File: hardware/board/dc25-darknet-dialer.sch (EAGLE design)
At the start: 62 parts

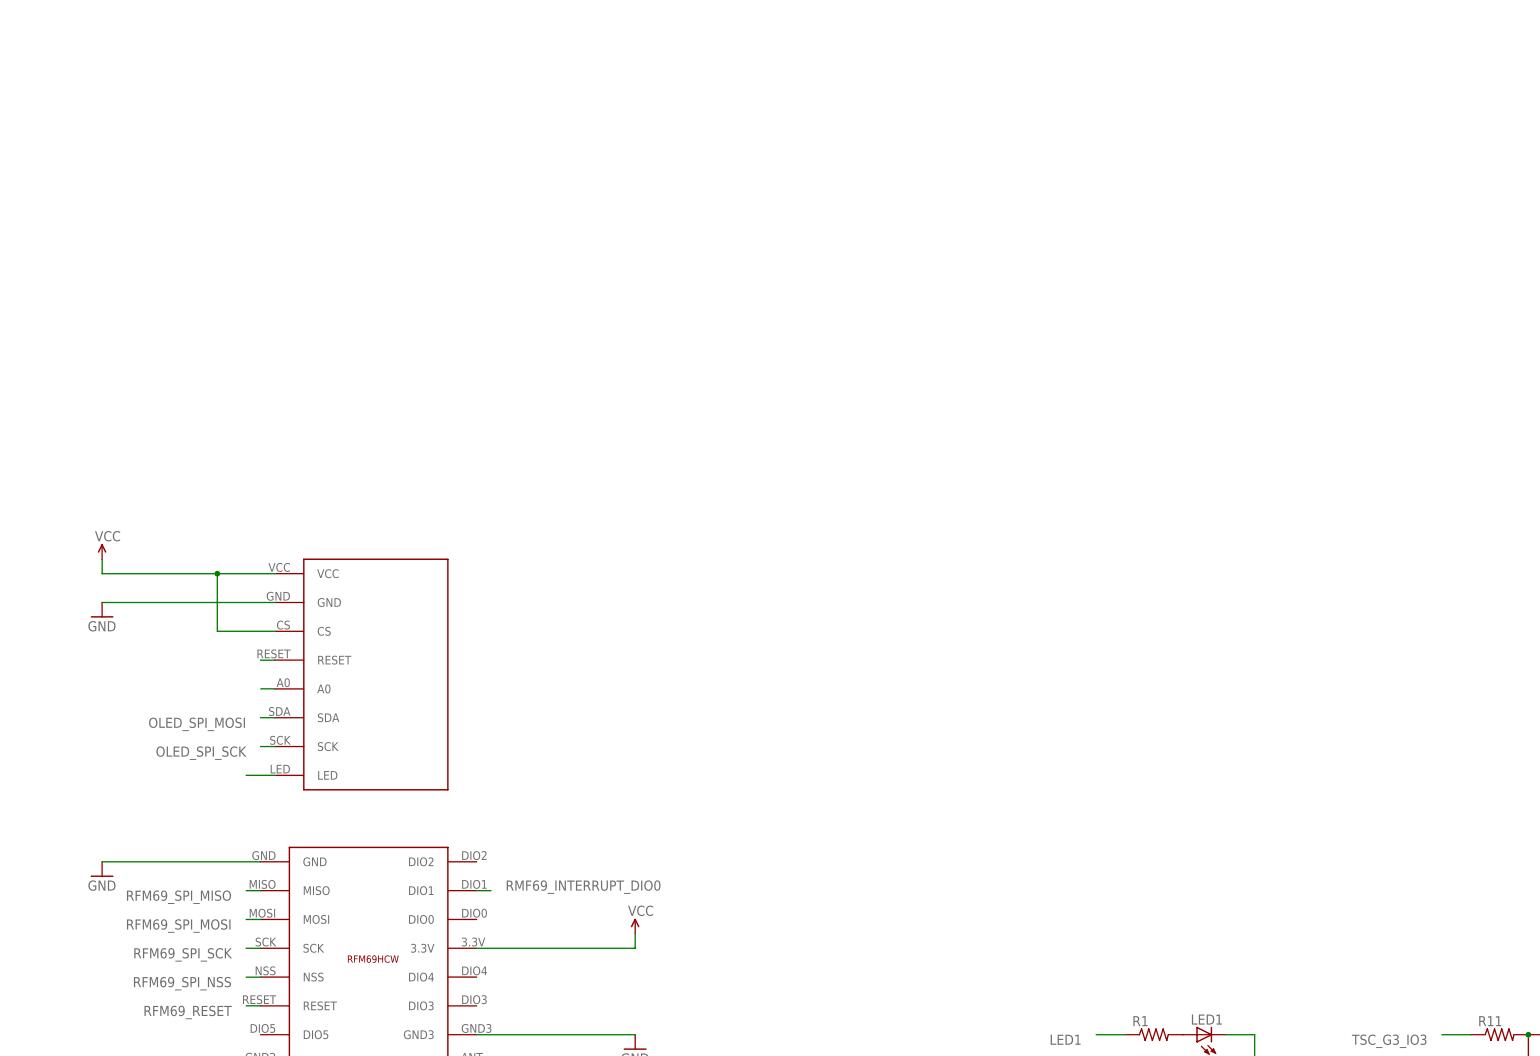
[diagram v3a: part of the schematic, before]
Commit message: Added power and IR
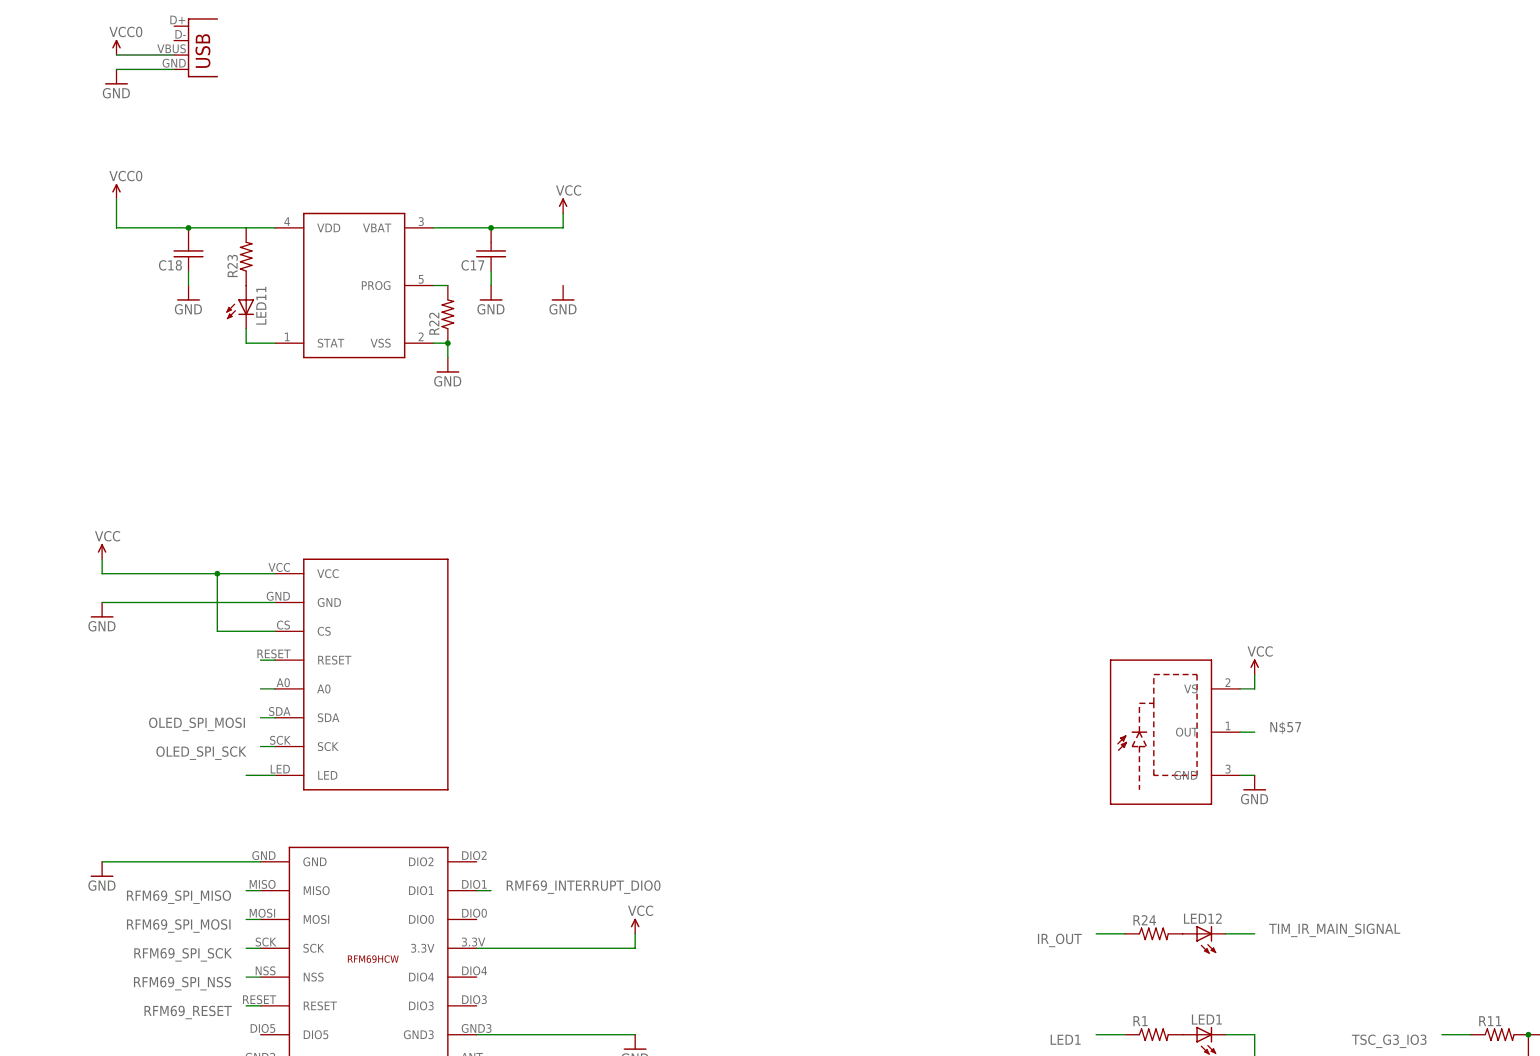
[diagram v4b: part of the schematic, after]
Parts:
- added C17, C18: (no value), SYNShop:C-USC0603
- added LED11: (no value), SYNShop:LED0603
- added LED12: (no value), SYNShop:LED5MM
- added R22, R23: (no value), SYNShop:R-US_R0603
- added R24: (no value), SYNShop:R-US_0309/12
- added U$11: DS21984E, darknet_parts_library:DS21984E
- added U$17: SOP22, SYNShop:SOP22
- added X1: USB-MICROB, SYNShop:USB-MICROB
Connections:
- new net N$22: R22.2, U$11.PROG
- new net N$23: LED12.A, R24.2
- new net N$24: LED11.A, R23.1
- new net N$25: LED11.C, U$11.STAT
- new net VCC0: C18.2, R23.2, U$11.VDD, X1.VBUS
- net GND: now also C17.1, C18.1, R22.1, U$11.VSS, U$17.GND, X1.GND
- net IR_OUT: now also R24.1
- net N$57: now also U$17.OUT
- net TIM_IR_MAIN_SIGNAL: now also LED12.C
- net VCC: now also C17.2, U$11.VBAT, U$17.VS
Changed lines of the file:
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@@
 <part name="U$10" library="SYNShop" deviceset="VCC" device=""/>
 <part name="C16" library="SYNShop" deviceset="C-US" device="C0603" value="4.7uF"/>
+<part name="U$11" library="darknet_parts_library" deviceset="DS21984E" device=""/>
+<part name="R22" library="SYNShop" deviceset="R-US_" device="R0603"/>
+<part name="GND22" library="SYNShop" deviceset="GND" device=""/>
+<part name="GND23" library="SYNShop" deviceset="GND" device=""/>
+<part name="R23" library="SYNShop" deviceset="R-US_" device="R0603"/>
+<part name="LED11" library="SYNShop" deviceset="LED" device="0603"/>
+<part name="C17" library="SYNShop" deviceset="C-US" device="C0603"/>
+<part name="GND24" library="SYNShop" deviceset="GND" device=""/>
+<part name="U$13" library="SYNShop" deviceset="VCC" device=""/>
+<part name="U$14" library="SYNShop" deviceset="VCC0" device=""/>
+<part name="C18" library="SYNShop" deviceset="C-US" device="C0603"/>
+<part name="GND25" library="SYNShop" deviceset="GND" device=""/>
+<part name="X1" library="SYNShop" deviceset="USB" device="-MICROB"/>
+<part name="U$16" library="SYNShop" deviceset="VCC0" device=""/>
+<part name="GND26" library="SYNShop" deviceset="GND" device=""/>
+<part name="U$17" library="SYNShop" deviceset="SOP22" device=""/>
+<part name="LED12" library="SYNShop" deviceset="LED" device="5MM"/>
+<part name="R24" library="SYNShop" deviceset="R-US_" device="0309/12"/>
+<part name="GND27" library="SYNShop" deviceset="GND" device=""/>
+<part name="U$18" library="SYNShop" deviceset="VCC" device=""/>
 </parts>
 <sheets>
@@
 <instance part="U$10" gate="G$1" x="114.3" y="144.78"/>
 <instance part="C16" gate="G$1" x="73.66" y="139.7" rot="R180"/>
+<instance part="U$11" gate="G$1" x="43.18" y="322.58"/>
+<instance part="R22" gate="G$1" x="58.42" y="317.5" rot="R90"/>
+<instance part="GND22" gate="1" x="58.42" y="307.34"/>
+<instance part="GND23" gate="1" x="66.04" y="320.04"/>
+<instance part="R23" gate="G$1" x="22.86" y="327.66" rot="R90"/>
+<instance part="LED11" gate="G$1" x="22.86" y="320.04"/>
+<instance part="C17" gate="G$1" x="66.04" y="327.66" rot="R180"/>
+<instance part="GND24" gate="1" x="78.74" y="320.04"/>
+<instance part="U$13" gate="G$1" x="78.74" y="335.28"/>
+<instance part="U$14" gate="VCC0" x="0" y="337.82"/>
+<instance part="C18" gate="G$1" x="12.7" y="327.66" rot="R180"/>
+<instance part="GND25" gate="1" x="12.7" y="320.04"/>
+<instance part="X1" gate="G$1" x="12.7" y="360.68"/>
+<instance part="U$16" gate="VCC0" x="0" y="363.22"/>
+<instance part="GND26" gate="1" x="0" y="358.14"/>
+<instance part="U$17" gate="G$1" x="185.42" y="243.84"/>
+<instance part="LED12" gate="G$1" x="190.5" y="208.28" rot="R90"/>
+<instance part="R24" gate="G$1" x="182.88" y="208.28"/>
+<instance part="GND27" gate="1" x="200.66" y="233.68"/>
+<instance part="U$18" gate="G$1" x="200.66" y="254"/>
 </instances>
 <busses>
@@
 <junction x="83.82" y="137.16"/>
 </segment>
+<segment>
+<pinref part="U$11" gate="G$1" pin="VSS"/>
+<pinref part="R22" gate="G$1" pin="1"/>
+<wire x1="55.88" y1="312.42" x2="58.42" y2="312.42" width="0.1524" layer="91"/>
+<pinref part="GND22" gate="1" pin="GND"/>
+<wire x1="58.42" y1="312.42" x2="58.42" y2="309.88" width="0.1524" layer="91"/>
+<junction x="58.42" y="312.42"/>
+</segment>
+<segment>
+<pinref part="C17" gate="G$1" pin="1"/>
+<pinref part="GND23" gate="1" pin="GND"/>
+<wire x1="66.04" y1="322.58" x2="66.04" y2="325.12" width="0.1524" layer="91"/>
+</segment>
+<segment>
+<pinref part="C18" gate="G$1" pin="1"/>
+<pinref part="GND25" gate="1" pin="GND"/>
+<wire x1="12.7" y1="322.58" x2="12.7" y2="325.12" width="0.1524" layer="91"/>
+</segment>
+<segment>
+<pinref part="X1" gate="G$1" pin="GND"/>
+<pinref part="GND26" gate="1" pin="GND"/>
+<wire x1="10.16" y1="360.68" x2="0" y2="360.68" width="0.1524" layer="91"/>
+</segment>
+<segment>
+<pinref part="U$17" gate="G$1" pin="GND"/>
+<pinref part="GND27" gate="1" pin="GND"/>
+<wire x1="198.12" y1="236.22" x2="200.66" y2="236.22" width="0.1524" layer="91"/>
+</segment>
 </net>
 <net name="N$12" class="0">
@@
 <junction x="83.82" y="144.78"/>
 </segment>
+<segment>
+<pinref part="U$11" gate="G$1" pin="VBAT"/>
+<wire x1="55.88" y1="332.74" x2="66.04" y2="332.74" width="0.1524" layer="91"/>
+<pinref part="C17" gate="G$1" pin="2"/>
+<wire x1="66.04" y1="332.74" x2="78.74" y2="332.74" width="0.1524" layer="91"/>
+<junction x="66.04" y="332.74"/>
+<pinref part="U$13" gate="G$1" pin="VCC"/>
+<wire x1="78.74" y1="332.74" x2="78.74" y2="335.28" width="0.1524" layer="91"/>
+</segment>
+<segment>
+<pinref part="U$17" gate="G$1" pin="VS"/>
+<pinref part="U$18" gate="G$1" pin="VCC"/>
+<wire x1="198.12" y1="251.46" x2="200.66" y2="251.46" width="0.1524" layer="91"/>
+<wire x1="200.66" y1="251.46" x2="200.66" y2="254" width="0.1524" layer="91"/>
+</segment>
 </net>
 <net name="TSC_G3_IO2" class="0">
@@
 <label x="15.24" y="137.16" size="1.778" layer="95" rot="R90"/>
 </segment>
+<segment>
+<pinref part="R24" gate="G$1" pin="1"/>
+<wire x1="177.8" y1="208.28" x2="172.72" y2="208.28" width="0.1524" layer="91"/>
+<label x="170.18" y="208.28" size="1.778" layer="95" rot="R180"/>
+</segment>
 </net>
 <net name="RCC_OSC_IN" class="0">
@@
 <label x="17.78" y="137.16" size="1.778" layer="95" rot="R90"/>
 </segment>
+<segment>
+<pinref part="LED12" gate="G$1" pin="C"/>
+<wire x1="195.58" y1="208.28" x2="200.66" y2="208.28" width="0.1524" layer="91"/>
+<label x="203.2" y="208.28" size="1.778" layer="95"/>
+</segment>
 </net>
 <net name="TSC_G5_IO4" class="0">
@@
 <label x="-10.16" y="99.06" size="1.778" layer="95" rot="R180"/>
 </segment>
+<segment>
+<pinref part="U$17" gate="G$1" pin="OUT"/>
+<wire x1="198.12" y1="243.84" x2="200.66" y2="243.84" width="0.1524" layer="91"/>
+<label x="203.2" y="243.84" size="1.778" layer="95"/>
+</segment>
 </net>
 <net name="N$58" class="0">
@@
 </segment>
 </net>
+<net name="N$22" class="0">
+<segment>
+<pinref part="U$11" gate="G$1" pin="PROG"/>
+<pinref part="R22" gate="G$1" pin="2"/>
+<wire x1="55.88" y1="322.58" x2="58.42" y2="322.58" width="0.1524" layer="91"/>
+</segment>
+</net>
+<net name="N$24" class="0">
+<segment>
+<pinref part="R23" gate="G$1" pin="1"/>
+<pinref part="LED11" gate="G$1" pin="A"/>
+</segment>
+</net>
+<net name="N$25" class="0">
+<segment>
+<pinref part="LED11" gate="G$1" pin="C"/>
+<wire x1="22.86" y1="314.96" x2="22.86" y2="312.42" width="0.1524" layer="91"/>
+<pinref part="U$11" gate="G$1" pin="STAT"/>
+<wire x1="22.86" y1="312.42" x2="27.94" y2="312.42" width="0.1524" layer="91"/>
+</segment>
+</net>
+<net name="VCC0" class="0">
+<segment>
+<pinref part="U$11" gate="G$1" pin="VDD"/>
+<pinref part="R23" gate="G$1" pin="2"/>
+<wire x1="27.94" y1="332.74" x2="22.86" y2="332.74" width="0.1524" layer="91"/>
+<wire x1="22.86" y1="332.74" x2="12.7" y2="332.74" width="0.1524" layer="91"/>
+<pinref part="C18" gate="G$1" pin="2"/>
+<junction x="12.7" y="332.74"/>
+<wire x1="12.7" y1="332.74" x2="0" y2="332.74" width="0.1524" layer="91"/>
+<pinref part="U$14" gate="VCC0" pin="VCC0"/>
+<wire x1="0" y1="332.74" x2="0" y2="337.82" width="0.1524" layer="91"/>
+</segment>
+<segment>
+<pinref part="U$16" gate="VCC0" pin="VCC0"/>
+<pinref part="X1" gate="G$1" pin="VBUS"/>
+<wire x1="0" y1="363.22" x2="10.16" y2="363.22" width="0.1524" layer="91"/>
+</segment>
+</net>
+<net name="N$23" class="0">
+<segment>
+<pinref part="R24" gate="G$1" pin="2"/>
+<pinref part="LED12" gate="G$1" pin="A"/>
+</segment>
+</net>

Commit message: Updated power, wired IR
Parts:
- added C19, C20: (no value), SYNShop:C-USC0603
- added CN1: (no value), adafruit:JST_2PIN-THM-RA
- added L1: (no value), dp_devices:FERRITE-0603
- added R25: (no value), SYNShop:R-US_0309/12
- added R26, R27: (no value), SYNShop:R-US_R0603
- added SW1: RESET, SYNShop:SWITCH_TACTILETACTILE-2PIN-NARROW
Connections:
- new net N$26: C19.2, R27.1, X1.D+
- new net N$27: C20.2, R26.1, X1.D-
- new net N$28: L1.2, X1.VBUS
- net GND: now also C19.1, C20.1, CN1.2, SW1.C
- net RESET: now also R25.1, SW1.A
- net VCC: now also CN1.1, R25.2
- net VCC0: now also L1.1; no longer X1.VBUS
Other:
- note added: "Note need to check on power connection / battery"
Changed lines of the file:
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@@
 <part name="X1" library="SYNShop" deviceset="USB" device="-MICROB"/>
 <part name="U$16" library="SYNShop" deviceset="VCC0" device=""/>
-<part name="GND26" library="SYNShop" deviceset="GND" device=""/>
 <part name="U$17" library="SYNShop" deviceset="SOP22" device=""/>
 <part name="LED12" library="SYNShop" deviceset="LED" device="5MM"/>
@@
 <part name="GND27" library="SYNShop" deviceset="GND" device=""/>
 <part name="U$18" library="SYNShop" deviceset="VCC" device=""/>
+<part name="CN1" library="adafruit" deviceset="JST_2PIN" device="-THM-RA"/>
+<part name="SW1" library="SYNShop" deviceset="SWITCH_TACTILE" device="TACTILE-2PIN-NARROW" value="RESET"/>
+<part name="R25" library="SYNShop" deviceset="R-US_" device="0309/12"/>
+<part name="GND28" library="SYNShop" deviceset="GND" device=""/>
+<part name="U$20" library="SYNShop" deviceset="VCC" device=""/>
+<part name="R26" library="SYNShop" deviceset="R-US_" device="R0603"/>
+<part name="R27" library="SYNShop" deviceset="R-US_" device="R0603"/>
+<part name="C19" library="SYNShop" deviceset="C-US" device="C0603"/>
+<part name="C20" library="SYNShop" deviceset="C-US" device="C0603"/>
+<part name="L1" library="dp_devices" deviceset="FERRITE" device="-0603"/>
+<part name="GND26" library="SYNShop" deviceset="GND" device=""/>
 </parts>
 <sheets>
 <sheet>
 <plain>
+<text x="99.06" y="317.5" size="1.778" layer="91">Note need to check on power connection / battery</text>
 </plain>
 <instances>
@@
 <instance part="C18" gate="G$1" x="12.7" y="327.66" rot="R180"/>
 <instance part="GND25" gate="1" x="12.7" y="320.04"/>
-<instance part="X1" gate="G$1" x="12.7" y="360.68"/>
-<instance part="U$16" gate="VCC0" x="0" y="363.22"/>
-<instance part="GND26" gate="1" x="0" y="358.14"/>
+<instance part="X1" gate="G$1" x="55.88" y="360.68"/>
+<instance part="U$16" gate="VCC0" x="0" y="365.76"/>
 <instance part="U$17" gate="G$1" x="185.42" y="243.84"/>
 <instance part="LED12" gate="G$1" x="190.5" y="208.28" rot="R90"/>
@@
 <instance part="GND27" gate="1" x="200.66" y="233.68"/>
 <instance part="U$18" gate="G$1" x="200.66" y="254"/>
+<instance part="CN1" gate="G$1" x="104.14" y="330.2"/>
+<instance part="SW1" gate="G$1" x="27.94" y="396.24"/>
+<instance part="R25" gate="G$1" x="27.94" y="406.4" rot="R90"/>
+<instance part="GND28" gate="1" x="27.94" y="388.62"/>
+<instance part="U$20" gate="G$1" x="27.94" y="411.48"/>
+<instance part="R26" gate="G$1" x="17.78" y="375.92" rot="R180"/>
+<instance part="R27" gate="G$1" x="17.78" y="381" rot="R180"/>
+<instance part="C19" gate="G$1" x="33.02" y="368.3" rot="R180"/>
+<instance part="C20" gate="G$1" x="25.4" y="368.3" rot="R180"/>
+<instance part="L1" gate="L" x="15.24" y="363.22" rot="R90"/>
+<instance part="GND26" gate="1" x="33.02" y="355.6"/>
 </instances>
 <busses>
@@
 </segment>
 <segment>
-<pinref part="X1" gate="G$1" pin="GND"/>
-<pinref part="GND26" gate="1" pin="GND"/>
-<wire x1="10.16" y1="360.68" x2="0" y2="360.68" width="0.1524" layer="91"/>
-</segment>
-<segment>
 <pinref part="U$17" gate="G$1" pin="GND"/>
 <pinref part="GND27" gate="1" pin="GND"/>
 <wire x1="198.12" y1="236.22" x2="200.66" y2="236.22" width="0.1524" layer="91"/>
 </segment>
+<segment>
+<pinref part="CN1" gate="G$1" pin="2"/>
+<pinref part="GND24" gate="1" pin="GND"/>
+<wire x1="101.6" y1="330.2" x2="78.74" y2="330.2" width="0.1524" layer="91"/>
+<wire x1="78.74" y1="330.2" x2="78.74" y2="322.58" width="0.1524" layer="91"/>
+</segment>
+<segment>
+<pinref part="X1" gate="G$1" pin="GND"/>
+<wire x1="53.34" y1="360.68" x2="33.02" y2="360.68" width="0.1524" layer="91"/>
+<pinref part="C20" gate="G$1" pin="1"/>
+<wire x1="33.02" y1="360.68" x2="25.4" y2="360.68" width="0.1524" layer="91"/>
+<wire x1="25.4" y1="365.76" x2="25.4" y2="360.68" width="0.1524" layer="91"/>
+<pinref part="C19" gate="G$1" pin="1"/>
+<wire x1="33.02" y1="365.76" x2="33.02" y2="360.68" width="0.1524" layer="91"/>
+<junction x="33.02" y="360.68"/>
+<pinref part="GND26" gate="1" pin="GND"/>
+<wire x1="33.02" y1="358.14" x2="33.02" y2="360.68" width="0.1524" layer="91"/>
+</segment>
+<segment>
+<pinref part="GND28" gate="1" pin="GND"/>
+<pinref part="SW1" gate="G$1" pin="C"/>
+</segment>
 </net>
 <net name="N$12" class="0">
@@
 <wire x1="-5.08" y1="101.6" x2="-7.62" y2="101.6" width="0.1524" layer="91"/>
 <label x="-10.16" y="101.6" size="1.778" layer="95" rot="R180"/>
+</segment>
+<segment>
+<pinref part="R25" gate="G$1" pin="1"/>
+<pinref part="SW1" gate="G$1" pin="A"/>
+<wire x1="27.94" y1="401.32" x2="48.26" y2="401.32" width="0.1524" layer="91"/>
+<label x="50.8" y="401.32" size="1.778" layer="95"/>
 </segment>
 </net>
@@
 <pinref part="U$13" gate="G$1" pin="VCC"/>
 <wire x1="78.74" y1="332.74" x2="78.74" y2="335.28" width="0.1524" layer="91"/>
+<pinref part="CN1" gate="G$1" pin="1"/>
+<wire x1="78.74" y1="332.74" x2="101.6" y2="332.74" width="0.1524" layer="91"/>
 </segment>
 <segment>
@@
 <wire x1="198.12" y1="251.46" x2="200.66" y2="251.46" width="0.1524" layer="91"/>
 <wire x1="200.66" y1="251.46" x2="200.66" y2="254" width="0.1524" layer="91"/>
+</segment>
+<segment>
+<pinref part="R25" gate="G$1" pin="2"/>
+<pinref part="U$20" gate="G$1" pin="VCC"/>
 </segment>
 </net>
@@
 </segment>
 <segment>
+<pinref part="L1" gate="L" pin="1"/>
 <pinref part="U$16" gate="VCC0" pin="VCC0"/>
-<pinref part="X1" gate="G$1" pin="VBUS"/>
-<wire x1="0" y1="363.22" x2="10.16" y2="363.22" width="0.1524" layer="91"/>
+<wire x1="7.62" y1="363.22" x2="0" y2="363.22" width="0.1524" layer="91"/>
+<wire x1="0" y1="363.22" x2="0" y2="365.76" width="0.1524" layer="91"/>
 </segment>
 </net>
@@
 </segment>
 </net>
+<net name="N$26" class="0">
+<segment>
+<pinref part="X1" gate="G$1" pin="D+"/>
+<pinref part="R27" gate="G$1" pin="1"/>
+<wire x1="22.86" y1="381" x2="33.02" y2="381" width="0.1524" layer="91"/>
+<wire x1="33.02" y1="381" x2="40.64" y2="381" width="0.1524" layer="91"/>
+<wire x1="40.64" y1="381" x2="40.64" y2="368.3" width="0.1524" layer="91"/>
+<wire x1="40.64" y1="368.3" x2="53.34" y2="368.3" width="0.1524" layer="91"/>
+<pinref part="C19" gate="G$1" pin="2"/>
+<wire x1="33.02" y1="373.38" x2="33.02" y2="381" width="0.1524" layer="91"/>
+<junction x="33.02" y="381"/>
+</segment>
+</net>
+<net name="N$27" class="0">
+<segment>
+<pinref part="X1" gate="G$1" pin="D-"/>
+<pinref part="R26" gate="G$1" pin="1"/>
+<wire x1="22.86" y1="375.92" x2="25.4" y2="375.92" width="0.1524" layer="91"/>
+<wire x1="25.4" y1="375.92" x2="38.1" y2="375.92" width="0.1524" layer="91"/>
+<wire x1="38.1" y1="375.92" x2="38.1" y2="365.76" width="0.1524" layer="91"/>
+<wire x1="38.1" y1="365.76" x2="53.34" y2="365.76" width="0.1524" layer="91"/>
+<pinref part="C20" gate="G$1" pin="2"/>
+<wire x1="25.4" y1="373.38" x2="25.4" y2="375.92" width="0.1524" layer="91"/>
+<junction x="25.4" y="375.92"/>
+</segment>
+</net>
+<net name="N$28" class="0">
+<segment>
+<pinref part="X1" gate="G$1" pin="VBUS"/>
+<pinref part="L1" gate="L" pin="2"/>
+<wire x1="53.34" y1="363.22" x2="22.86" y2="363.22" width="0.1524" layer="91"/>
+</segment>
+</net>
